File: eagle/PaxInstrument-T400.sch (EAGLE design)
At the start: 123 parts, among them IC1 MCP3424, U1 MCP9800, U3 MCP73831, U4 MIC5219-3.3V, U7 USD-SOCKETNEW, U8 NC7S32, X1 FH12-12S-0.5SH, Y1 RESONATORSMD

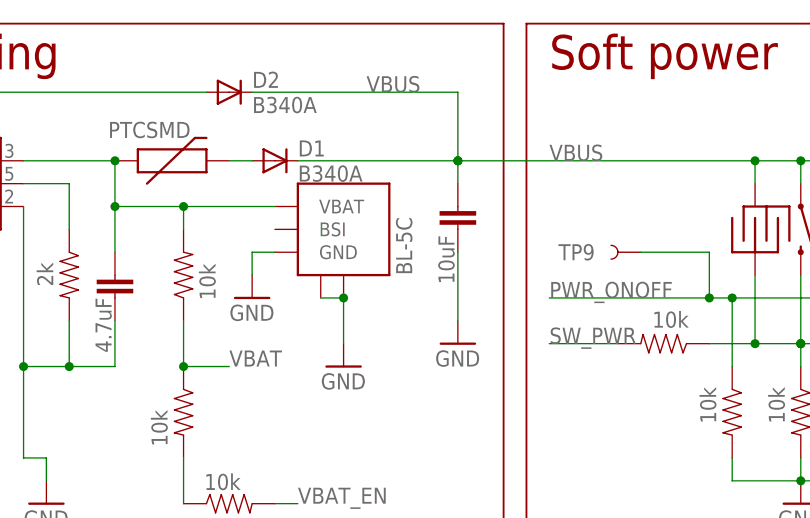
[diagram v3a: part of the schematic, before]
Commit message: - All items on the board should stay as-is
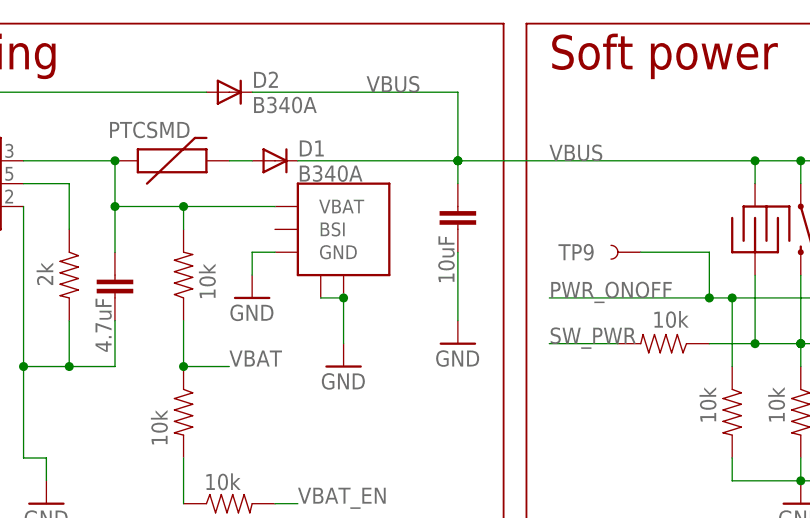
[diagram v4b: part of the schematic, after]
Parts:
- removed U$6: BL-5C-OUTLINE, charlespax:BL-5C-OUTLINE
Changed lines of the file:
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@@
 <grid distance="0.1" unitdist="inch" unit="inch" style="lines" multiple="1" display="no" altdistance="0.01" altunitdist="inch" altunit="inch"/>
 <layers>
-<layer number="1" name="Top" color="4" fill="1" visible="yes" active="no"/>
-<layer number="2" name="Route2" color="1" fill="3" visible="yes" active="no"/>
-<layer number="3" name="Route3" color="4" fill="3" visible="yes" active="no"/>
-<layer number="14" name="Route14" color="1" fill="6" visible="yes" active="no"/>
-<layer number="15" name="Route15" color="4" fill="6" visible="yes" active="no"/>
-<layer number="16" name="Bottom" color="1" fill="1" visible="yes" active="no"/>
-<layer number="17" name="Pads" color="2" fill="1" visible="yes" active="no"/>
-<layer number="18" name="Vias" color="2" fill="1" visible="yes" active="no"/>
-<layer number="19" name="Unrouted" color="6" fill="1" visible="yes" active="no"/>
-<layer number="20" name="Dimension" color="15" fill="1" visible="yes" active="no"/>
-<layer number="21" name="tPlace" color="16" fill="1" visible="yes" active="no"/>
-<layer number="22" name="bPlace" color="14" fill="1" visible="yes" active="no"/>
-<layer number="23" name="tOrigins" color="15" fill="1" visible="yes" active="no"/>
-<layer number="24" name="bOrigins" color="15" fill="1" visible="yes" active="no"/>
-<layer number="25" name="tNames" color="7" fill="1" visible="yes" active="no"/>
-<layer number="26" name="bNames" color="7" fill="1" visible="yes" active="no"/>
-<layer number="27" name="tValues" color="7" fill="1" visible="yes" active="no"/>
-<layer number="28" name="bValues" color="7" fill="1" visible="yes" active="no"/>
+<layer number="1" name="Top" color="4" fill="1" visible="no" active="no"/>
+<layer number="2" name="Route2" color="1" fill="3" visible="no" active="no"/>
+<layer number="3" name="Route3" color="4" fill="3" visible="no" active="no"/>
+<layer number="14" name="Route14" color="1" fill="6" visible="no" active="no"/>
+<layer number="15" name="Route15" color="4" fill="6" visible="no" active="no"/>
+<layer number="16" name="Bottom" color="1" fill="1" visible="no" active="no"/>
+<layer number="17" name="Pads" color="2" fill="1" visible="no" active="no"/>
+<layer number="18" name="Vias" color="2" fill="1" visible="no" active="no"/>
+<layer number="19" name="Unrouted" color="6" fill="1" visible="no" active="no"/>
+<layer number="20" name="Dimension" color="15" fill="1" visible="no" active="no"/>
+<layer number="21" name="tPlace" color="16" fill="1" visible="no" active="no"/>
+<layer number="22" name="bPlace" color="14" fill="1" visible="no" active="no"/>
+<layer number="23" name="tOrigins" color="15" fill="1" visible="no" active="no"/>
+<layer number="24" name="bOrigins" color="15" fill="1" visible="no" active="no"/>
+<layer number="25" name="tNames" color="7" fill="1" visible="no" active="no"/>
+<layer number="26" name="bNames" color="7" fill="1" visible="no" active="no"/>
+<layer number="27" name="tValues" color="7" fill="1" visible="no" active="no"/>
+<layer number="28" name="bValues" color="7" fill="1" visible="no" active="no"/>
 <layer number="29" name="tStop" color="7" fill="3" visible="no" active="no"/>
 <layer number="30" name="bStop" color="7" fill="6" visible="no" active="no"/>
@@
 <layer number="35" name="tGlue" color="7" fill="4" visible="no" active="no"/>
 <layer number="36" name="bGlue" color="7" fill="5" visible="no" active="no"/>
-<layer number="37" name="tTest" color="7" fill="1" visible="yes" active="no"/>
-<layer number="38" name="bTest" color="7" fill="1" visible="yes" active="no"/>
+<layer number="37" name="tTest" color="7" fill="1" visible="no" active="no"/>
+<layer number="38" name="bTest" color="7" fill="1" visible="no" active="no"/>
 <layer number="39" name="tKeepout" color="4" fill="11" visible="no" active="no"/>
 <layer number="40" name="bKeepout" color="1" fill="11" visible="no" active="no"/>
@@
 <layer number="44" name="Drills" color="7" fill="1" visible="no" active="no"/>
 <layer number="45" name="Holes" color="7" fill="1" visible="no" active="no"/>
-<layer number="46" name="Milling" color="3" fill="1" visible="yes" active="no"/>
-<layer number="47" name="Measures" color="7" fill="1" visible="yes" active="no"/>
-<layer number="48" name="Document" color="7" fill="1" visible="yes" active="no"/>
-<layer number="49" name="Reference" color="7" fill="1" visible="yes" active="no"/>
-<layer number="50" name="dxf" color="7" fill="1" visible="yes" active="no"/>
-<layer number="51" name="tDocu" color="6" fill="1" visible="yes" active="no"/>
-<layer number="52" name="bDocu" color="7" fill="1" visible="yes" active="no"/>
-<layer number="53" name="tGND_GNDA" color="7" fill="9" visible="yes" active="no"/>
-<layer number="54" name="bGND_GNDA" color="1" fill="9" visible="yes" active="no"/>
-<layer number="56" name="wert" color="7" fill="1" visible="yes" active="no"/>
+<layer number="46" name="Milling" color="3" fill="1" visible="no" active="no"/>
+<layer number="47" name="Measures" color="7" fill="1" visible="no" active="no"/>
+<layer number="48" name="Document" color="7" fill="1" visible="no" active="no"/>
+<layer number="49" name="Reference" color="7" fill="1" visible="no" active="no"/>
+<layer number="50" name="dxf" color="7" fill="1" visible="no" active="no"/>
+<layer number="51" name="tDocu" color="6" fill="1" visible="no" active="no"/>
+<layer number="52" name="bDocu" color="7" fill="1" visible="no" active="no"/>
+<layer number="53" name="tGND_GNDA" color="7" fill="9" visible="no" active="no"/>
+<layer number="54" name="bGND_GNDA" color="1" fill="9" visible="no" active="no"/>
+<layer number="56" name="wert" color="7" fill="1" visible="no" active="no"/>
 <layer number="91" name="Nets" color="2" fill="1" visible="yes" active="yes"/>
 <layer number="92" name="Busses" color="1" fill="1" visible="yes" active="yes"/>
@@
 <attribute name="OC_DIGIKEY" value="HFJ112TR-ND"/>
 </part>
-<part name="U$6" library="charlespax" deviceset="BL-5C-OUTLINE" device=""/>
 </parts>
 <sheets>
@@
 <attribute name="OC_DIGIKEY" x="297.18" y="238.76" size="1.778" layer="96" rot="MR180" display="off"/>
 </instance>
-<instance part="U$6" gate="G$1" x="144.78" y="226.06" rot="R90"/>
 </instances>
 <busses>

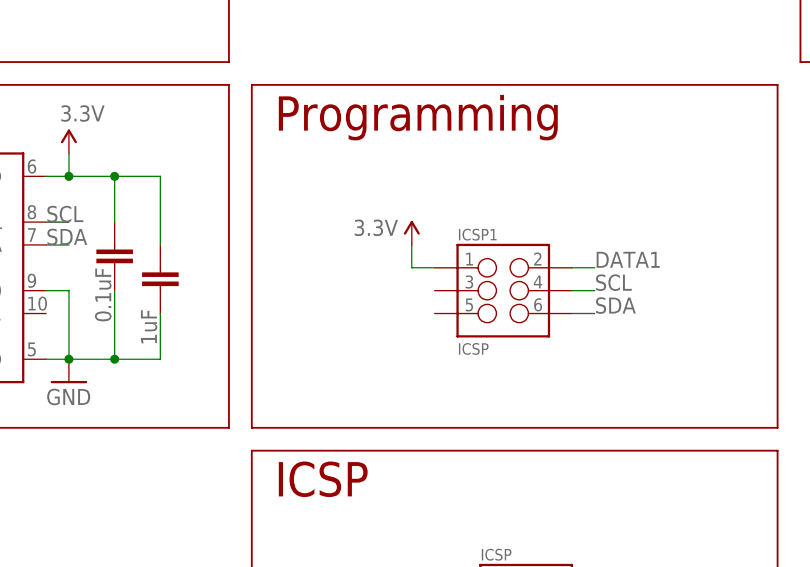
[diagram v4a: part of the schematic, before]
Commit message: - battery moved to correct location
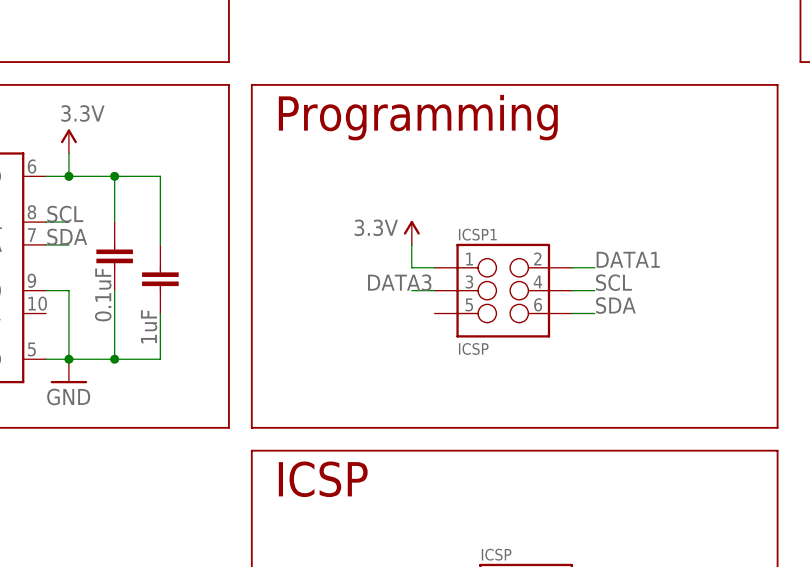
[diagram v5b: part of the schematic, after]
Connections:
- net DATA3: now also ICSP1.3
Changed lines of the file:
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@@
 <label x="83.82" y="139.7" size="1.778" layer="95"/>
+</segment>
+<segment>
+<pinref part="ICSP1" gate="G$1" pin="3"/>
+<wire x1="193.04" y1="88.9" x2="190.5" y2="88.9" width="0.1524" layer="91"/>
+<label x="185.42" y="88.9" size="1.778" layer="95"/>
 </segment>
 </net>

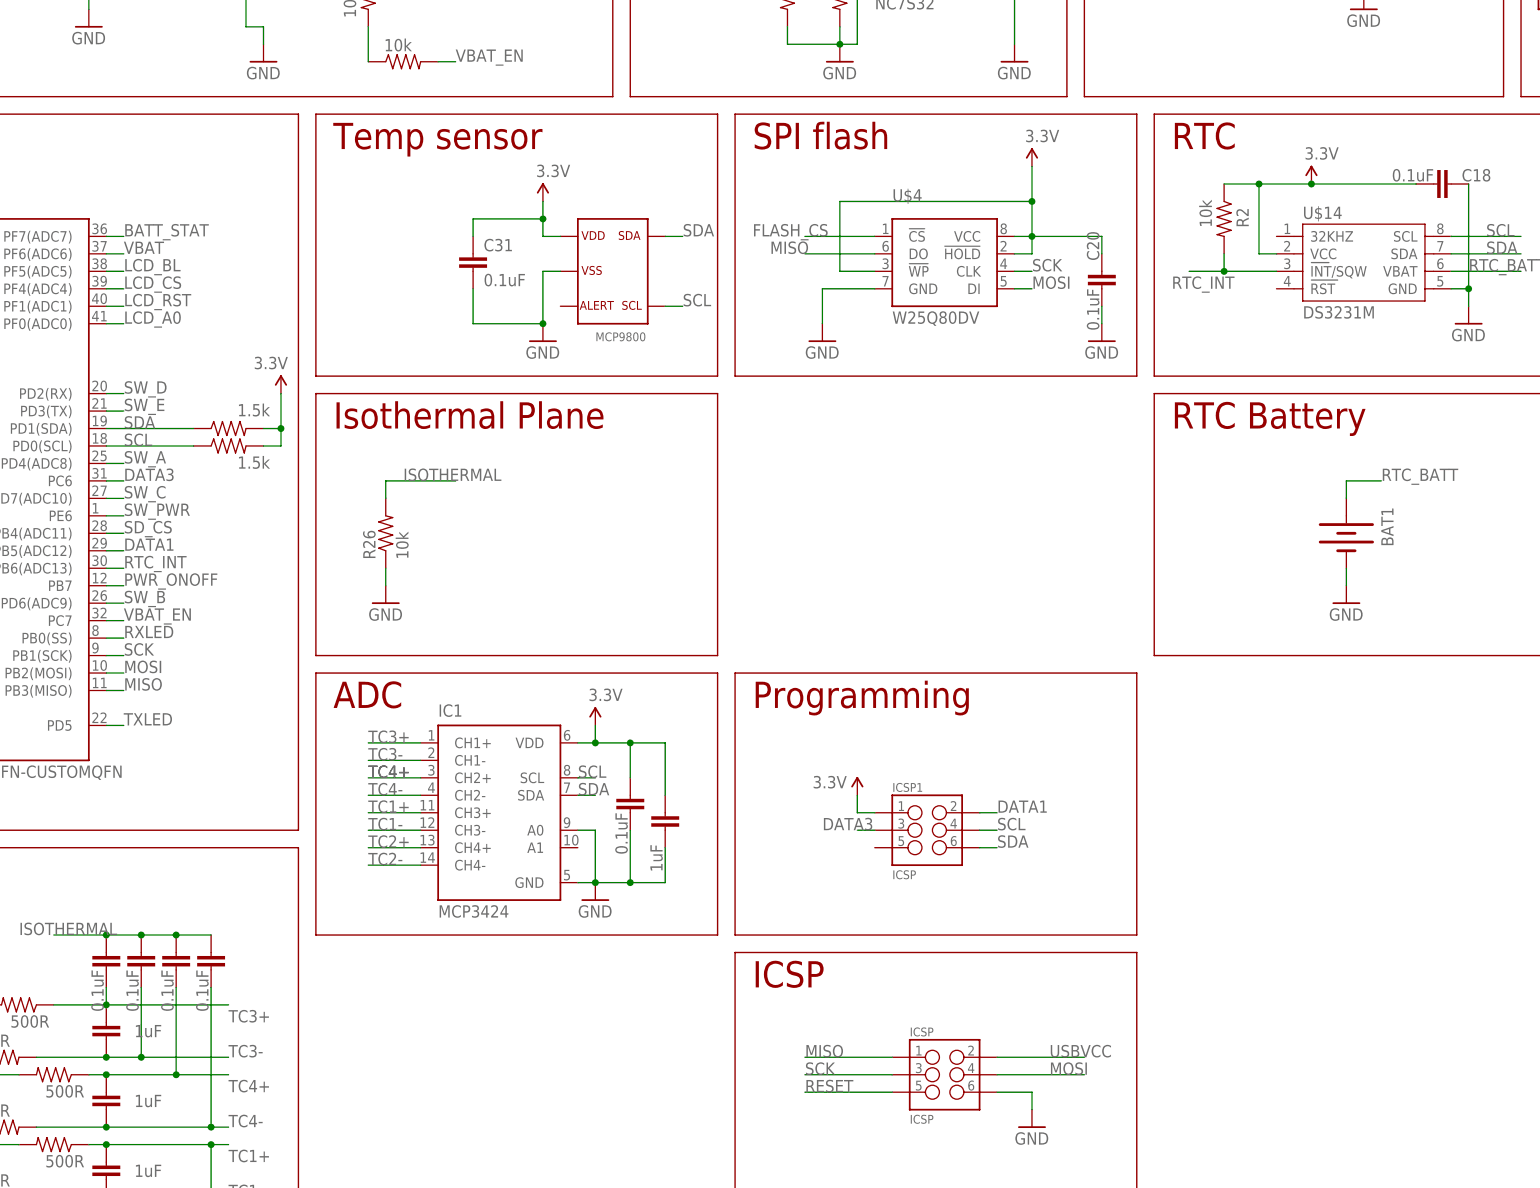
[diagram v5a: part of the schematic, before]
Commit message: PCB layout and schematic update by Sam
-Swapped I/O for PCB layout
-Swapped ADC channel for PCB layout
-Bug fixed Flash_CS pin unconnected and replaced DATA3
- ICSP changed USBVCC to N$20
- ICSP1 removed DATA3
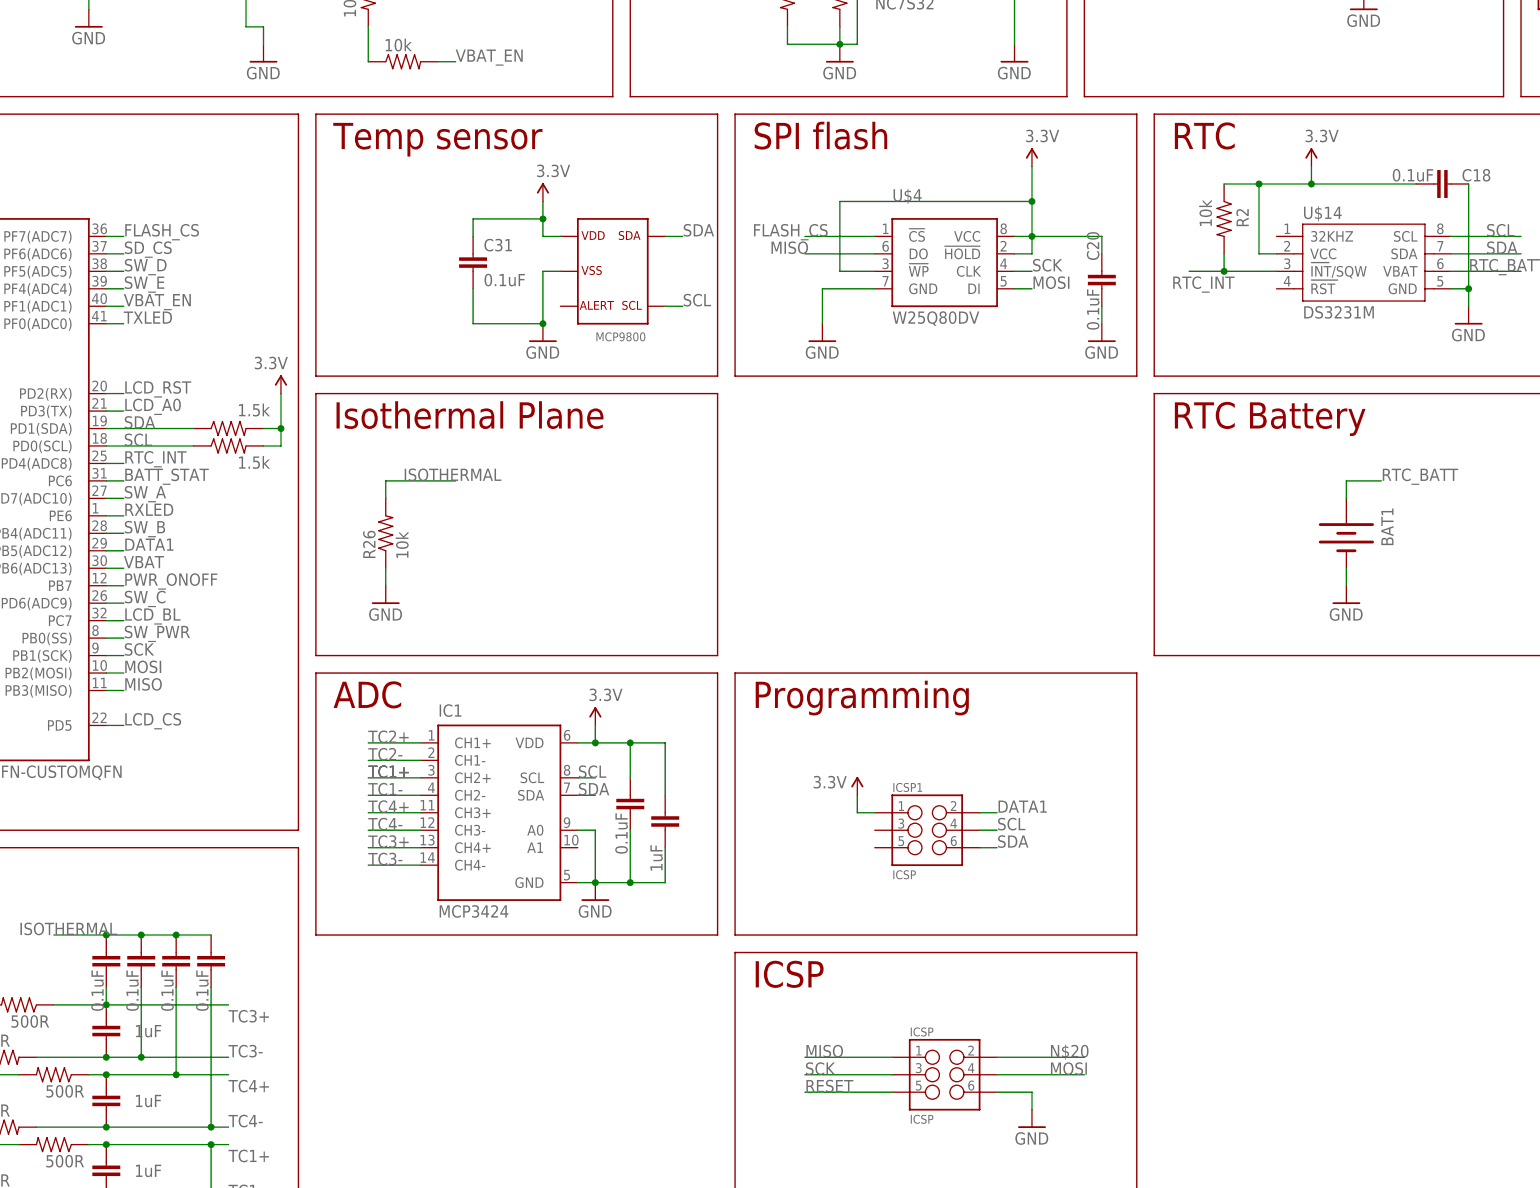
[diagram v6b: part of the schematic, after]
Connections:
- removed net DATA3: ICSP1.3, U$3.PC6
- net BATT_STAT: now also U$3.PC6; no longer U$3.PF7(ADC7)
- net FLASH_CS: now also U$3.PF7(ADC7)
- net LCD_A0: now also U$3.PD3(TX); no longer U$3.PF0(ADC0)
- net LCD_BL: now also U$3.PC7; no longer U$3.PF5(ADC5)
- net LCD_CS: now also U$3.PD5; no longer U$3.PF4(ADC4)
- net LCD_RST: now also U$3.PD2(RX); no longer U$3.PF1(ADC1)
- net N$20: now also ICSP.2
- net RTC_INT: now also U$3.PD4(ADC8); no longer U$3.PB6(ADC13)
- net RXLED: now also U$3.PE6; no longer U$3.PB0(SS)
- net SD_CS: now also U$3.PF6(ADC6); no longer U$3.PB4(ADC11)
- net SW_A: now also U$3.PD7(ADC10); no longer U$3.PD4(ADC8)
- net SW_B: now also U$3.PB4(ADC11); no longer U$3.PD6(ADC9)
- net SW_C: now also U$3.PD6(ADC9); no longer U$3.PD7(ADC10)
- net SW_D: now also U$3.PF5(ADC5); no longer U$3.PD2(RX)
- net SW_E: now also U$3.PF4(ADC4); no longer U$3.PD3(TX)
- net SW_PWR: now also U$3.PB0(SS); no longer U$3.PE6
- net TC1+: now also IC1.CH2+; no longer IC1.CH3+
- net TC1-: now also IC1.CH2-; no longer IC1.CH3-
- net TC2+: now also IC1.CH1+; no longer IC1.CH4+
- net TC2-: now also IC1.CH1-; no longer IC1.CH4-
- net TC3+: now also IC1.CH4+; no longer IC1.CH1+
- net TC3-: now also IC1.CH4-; no longer IC1.CH1-
- net TC4+: now also IC1.CH3+; no longer IC1.CH2+
- net TC4-: now also IC1.CH3-; no longer IC1.CH2-
- net TXLED: now also U$3.PF0(ADC0); no longer U$3.PD5
- net USBVCC: no longer ICSP.2
- net VBAT: now also U$3.PB6(ADC13); no longer U$3.PF6(ADC6)
- net VBAT_EN: now also U$3.PF1(ADC1); no longer U$3.PC7

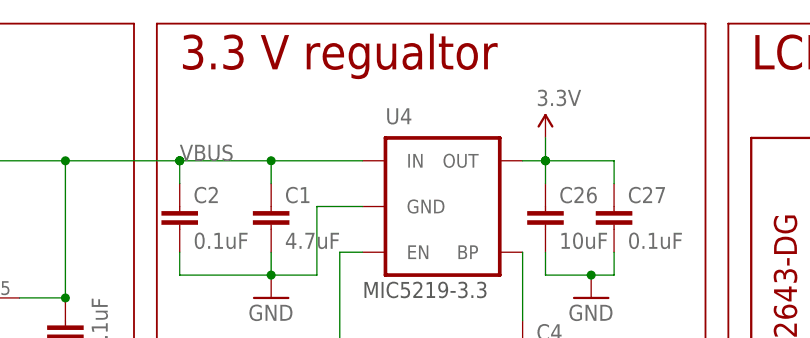
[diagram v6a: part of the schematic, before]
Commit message: fixed 'regulator' spelled wrong on schematic
Minor bug fixed in schematic
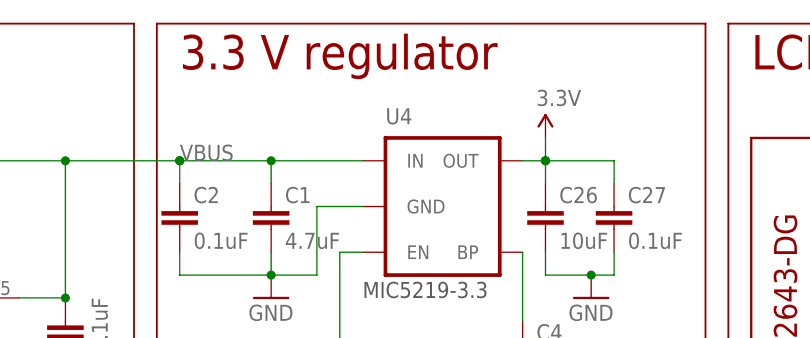
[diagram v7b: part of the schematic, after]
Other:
- note added: "3.3 V regulator"
- note removed: "3.3 V regualtor"
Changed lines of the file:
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@@
 <text x="66.04" y="248.92" size="3.81" layer="94">Battery charging</text>
 <text x="160.02" y="248.92" size="3.81" layer="94">Soft power</text>
-<text x="226.06" y="248.92" size="3.81" layer="94">3.3 V regualtor</text>
+<text x="226.06" y="248.92" size="3.81" layer="94">3.3 V regulator</text>
 <text x="236.22" y="187.96" size="3.81" layer="94">RTC</text>
 <wire x1="287.02" y1="254" x2="330.2" y2="254" width="0.2032" layer="94"/>
